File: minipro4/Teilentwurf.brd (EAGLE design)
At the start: 105.1 x 94.6 mm, 90 parts, among them IC1 MEGA8-P, IC2 FT232RL_ADAPTER, IC3 78L08Z, IC4 4051N, IC5 TL082P, IC6 4051N, IC7 TL082P, J1 HOHLSTECKER, Q2 BS170, Q3 BS170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

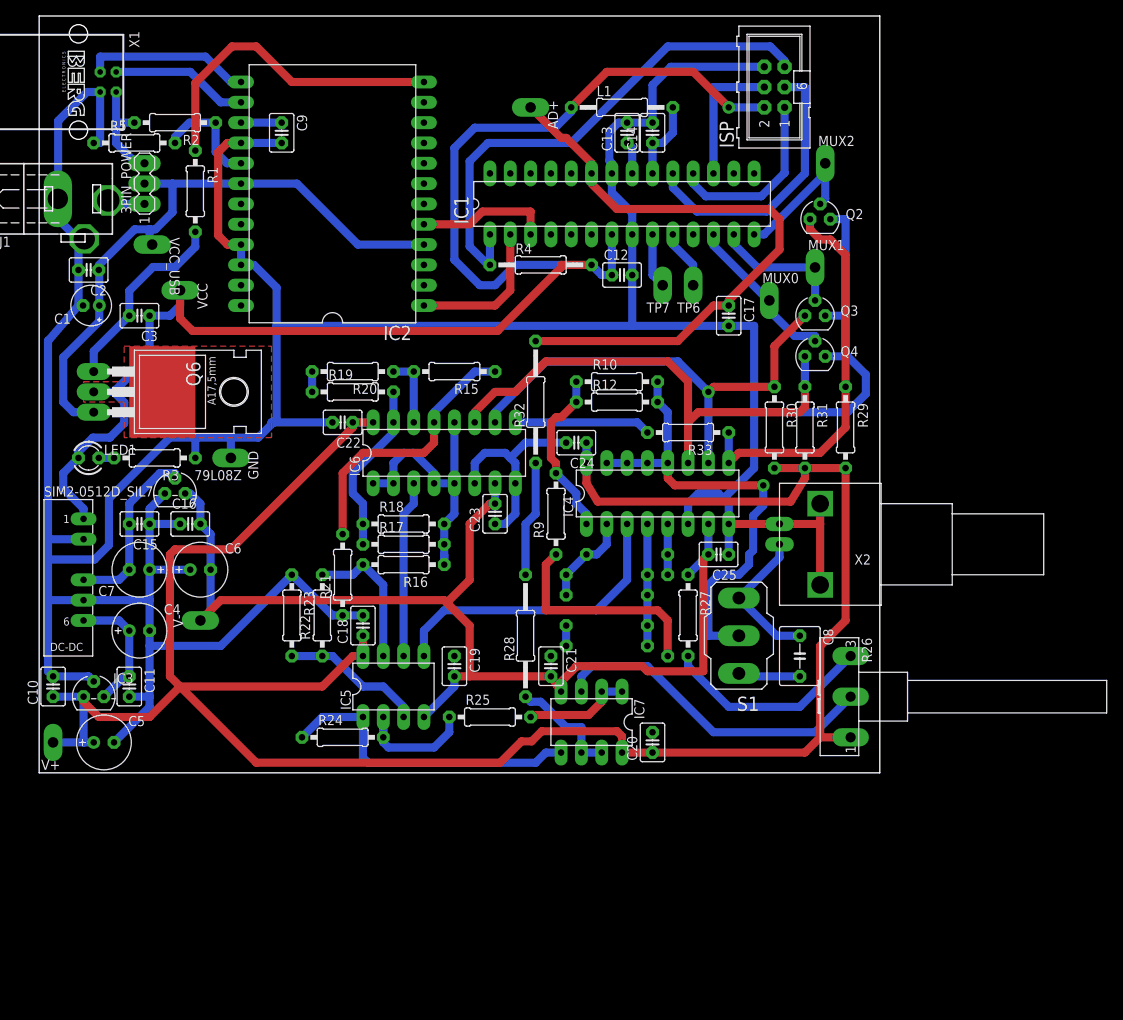
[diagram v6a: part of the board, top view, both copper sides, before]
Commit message: Added ground plane
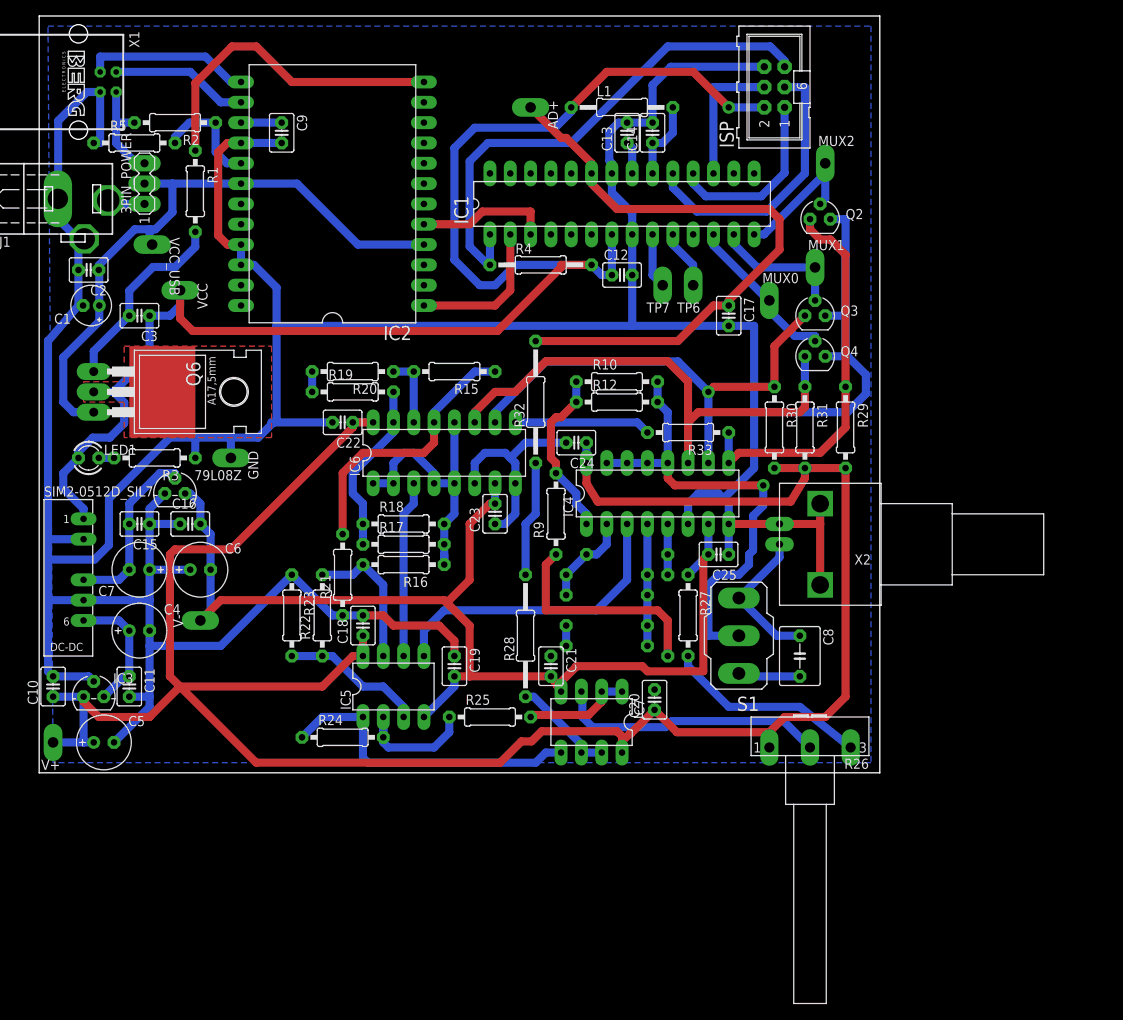
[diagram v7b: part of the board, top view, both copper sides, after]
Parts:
- moved R26 6.35 mm to (96.5, 2.54), turned to 90 degrees
- moved C20 5.34 mm to (77.1, 7.24)
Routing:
- net GND: track 531.0 -> 545.6 mm
- net N$39: track 41.3 -> 33.9 mm
- net V+: track 283.0 -> 281.7 mm
- net N$40: track 14.3 -> 13.0 mm
- net N$38: track 26.3 -> 25.5 mm
- added copper zone on layer 16, net GND
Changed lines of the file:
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@@
 <setting verticaltext="up"/>
 </settings>
-<grid distance="25" unitdist="mil" unit="mil" style="lines" multiple="1" display="no" altdistance="0.3175" altunitdist="mm" altunit="mm"/>
+<grid distance="10" unitdist="mil" unit="mil" style="lines" multiple="1" display="no" altdistance="0.3175" altunitdist="mm" altunit="mm"/>
 <layers>
 <layer number="1" name="Top" color="4" fill="1" visible="yes" active="yes"/>
@@
 <element name="IC7" library="03_device-library" package="DIL08" value="TL082P" x="69.215" y="4.445" rot="R180"/>
 <element name="R25" library="03_device-library" package="0207/10" value="100k" x="56.515" y="5.08"/>
-<element name="R26" library="03_device-library" package="POT" value="100k" x="100.33" y="7.62" rot="R180"/>
+<element name="R26" library="03_device-library" package="POT" value="100k" x="96.52" y="2.54" rot="R90"/>
 <element name="R27" library="03_device-library" package="0207/10" value="22k" x="81.28" y="17.78" rot="R270"/>
 <element name="R28" library="03_device-library" package="0207/15" value="8k2" x="60.96" y="15.24" rot="R90"/>
@@
 <element name="C18" library="03_device-library" package="C025-030X050" value="100nF" x="40.64" y="16.51" rot="R90"/>
 <element name="C19" library="03_device-library" package="C025-030X050" value="100nF" x="52.07" y="11.43" rot="R270"/>
-<element name="C20" library="03_device-library" package="C025-030X050" value="100nF" x="76.835" y="1.905" rot="R90"/>
+<element name="C20" library="03_device-library" package="C025-030X050" value="100nF" x="77.089" y="7.239" rot="R90"/>
 <element name="C21" library="03_device-library" package="C025-030X050" value="100nF" x="64.135" y="11.43" rot="R270"/>
 <element name="C22" library="03_device-library" package="C025-030X050" value="100nF" x="38.1" y="41.91" rot="R180"/>
@@
 <wire x1="59.69" y1="30.48" x2="58.42" y2="29.21" width="1.016" layer="16"/>
 <wire x1="58.42" y1="29.21" x2="57.15" y2="29.21" width="1.016" layer="16"/>
-<wire x1="66.04" y1="16.51" x2="58.42" y2="29.21" width="0" layer="19" extent="16-16"/>
-<wire x1="64.135" y1="12.7" x2="66.04" y2="13.97" width="0" layer="19" extent="1-1"/>
-<wire x1="52.07" y1="12.7" x2="64.135" y2="12.7" width="0" layer="19" extent="1-1"/>
-<wire x1="40.64" y1="17.78" x2="52.07" y2="12.7" width="0" layer="19" extent="1-1"/>
-<wire x1="76.835" y1="3.175" x2="66.04" y2="13.97" width="0" layer="19" extent="1-1"/>
+<polygon width="0.8128" layer="16" isolate="0.254" rank="2">
+<vertex x="1.27" y="91.44"/>
+<vertex x="104.14" y="91.44"/>
+<vertex x="104.14" y="-0.635"/>
+<vertex x="1.905" y="-0.635"/>
+</polygon>
+<wire x1="52.07" y1="12.7" x2="52.07" y2="14.605" width="1.016" layer="1"/>
+<wire x1="52.07" y1="14.605" x2="50.165" y2="16.51" width="1.016" layer="1"/>
+<wire x1="50.165" y1="16.51" x2="44.45" y2="16.51" width="1.016" layer="1"/>
+<wire x1="44.45" y1="16.51" x2="43.18" y2="17.78" width="1.016" layer="1"/>
+<wire x1="43.18" y1="17.78" x2="40.64" y2="17.78" width="1.016" layer="1"/>
 </signal>
 <signal name="N$20">
@@
 <wire x1="69.977" y1="32.004" x2="68.58" y2="34.29" width="1.016" layer="1"/>
 <wire x1="68.58" y1="34.29" x2="68.58" y2="36.83" width="1.016" layer="1"/>
-<wire x1="100.965" y1="36.195" x2="100.965" y2="17.145" width="1.016" layer="1"/>
-<wire x1="97.79" y1="13.97" x2="97.79" y2="2.54" width="1.016" layer="1"/>
-<wire x1="97.79" y1="2.54" x2="101.6" y2="2.54" width="1.016" layer="1"/>
-<wire x1="100.965" y1="17.145" x2="97.79" y2="13.97" width="1.016" layer="1"/>
+<wire x1="100.965" y1="36.195" x2="100.965" y2="7.62" width="1.016" layer="1"/>
 <wire x1="95.885" y1="36.195" x2="95.885" y2="34.925" width="1.016" layer="1"/>
 <wire x1="95.885" y1="34.925" x2="94.107" y2="32.004" width="1.016" layer="1"/>
@@
 <wire x1="16.51" y1="25.4" x2="16.51" y2="10.16" width="1.016" layer="1"/>
 <wire x1="16.51" y1="10.16" x2="17.78" y2="8.89" width="1.016" layer="1"/>
-<wire x1="76.835" y1="0.635" x2="95.885" y2="0.635" width="1.016" layer="1"/>
-<wire x1="95.885" y1="0.635" x2="97.79" y2="2.54" width="1.016" layer="1"/>
 <wire x1="39.37" y1="41.91" x2="39.37" y2="41.275" width="1.016" layer="1"/>
 <wire x1="39.37" y1="41.275" x2="24.13" y2="26.035" width="1.016" layer="1"/>
-<wire x1="73.025" y1="0.635" x2="73.025" y2="2.667" width="1.016" layer="1"/>
+<wire x1="73.025" y1="0.635" x2="73.025" y2="2.032" width="1.016" layer="1"/>
+<wire x1="73.025" y1="2.032" x2="73.025" y2="2.667" width="1.016" layer="1"/>
 <wire x1="60.452" y1="2.032" x2="57.785" y2="-0.635" width="1.016" layer="1"/>
 <wire x1="57.785" y1="-0.635" x2="27.305" y2="-0.635" width="1.016" layer="1"/>
 <wire x1="27.305" y1="-0.635" x2="17.78" y2="8.89" width="1.016" layer="1"/>
-<wire x1="73.025" y1="0.635" x2="76.835" y2="0.635" width="1.016" layer="1"/>
 <wire x1="73.025" y1="2.667" x2="72.39" y2="3.302" width="1.016" layer="1"/>
 <wire x1="72.39" y1="3.302" x2="62.992" y2="3.302" width="1.016" layer="1"/>
 <wire x1="62.992" y1="3.302" x2="61.722" y2="2.032" width="1.016" layer="1"/>
 <wire x1="61.722" y1="2.032" x2="60.452" y2="2.032" width="1.016" layer="1"/>
+<wire x1="91.44" y1="1.27" x2="91.44" y2="3.175" width="1.016" layer="1"/>
+<wire x1="91.44" y1="3.175" x2="93.345" y2="5.08" width="1.016" layer="1"/>
+<wire x1="100.965" y1="7.62" x2="98.425" y2="5.08" width="1.016" layer="1"/>
+<wire x1="98.425" y1="5.08" x2="93.345" y2="5.08" width="1.016" layer="1"/>
+<wire x1="77.089" y1="5.969" x2="74.168" y2="3.048" width="1.016" layer="1"/>
+<wire x1="74.168" y1="3.048" x2="74.041" y2="3.048" width="1.016" layer="1"/>
+<wire x1="74.041" y1="3.048" x2="73.025" y2="2.032" width="1.016" layer="1"/>
+<wire x1="91.44" y1="3.175" x2="79.883" y2="3.175" width="1.016" layer="1"/>
+<wire x1="79.883" y1="3.175" x2="77.089" y2="5.969" width="1.016" layer="1"/>
 </signal>
 <signal name="V-">
@@
 <wire x1="53.975" y1="29.21" x2="53.975" y2="22.225" width="1.016" layer="1"/>
 <wire x1="53.975" y1="22.225" x2="51.1175" y2="19.3675" width="1.016" layer="1"/>
-<wire x1="52.07" y1="10.16" x2="64.135" y2="10.16" width="1.016" layer="1"/>
+<wire x1="52.07" y1="10.16" x2="53.975" y2="10.16" width="1.016" layer="1"/>
+<wire x1="53.975" y1="10.16" x2="64.135" y2="10.16" width="1.016" layer="1"/>
 <wire x1="64.135" y1="10.16" x2="64.9165375" y2="8.98769375" width="1.016" layer="1"/>
 <wire x1="64.9165375" y1="8.98769375" x2="65.405" y2="8.255" width="1.016" layer="1"/>
@@
 <wire x1="67.31" y1="11.43" x2="67.31" y2="11.38115625" width="1.016" layer="1"/>
 <wire x1="67.31" y1="11.38115625" x2="64.9165375" y2="8.98769375" width="1.016" layer="1"/>
-<wire x1="53.975" y1="10.16" x2="52.07" y2="10.16" width="0" layer="19" extent="1-1"/>
 </signal>
 <signal name="N$4">
@@
 <wire x1="81.28" y1="12.7" x2="81.28" y2="11.43" width="1.016" layer="16"/>
 <wire x1="81.28" y1="11.43" x2="86.36" y2="6.35" width="1.016" layer="16"/>
-<wire x1="95.25" y1="6.35" x2="101.6" y2="12.7" width="1.016" layer="16"/>
+<wire x1="95.25" y1="6.35" x2="101.6" y2="1.27" width="1.016" layer="16"/>
 <wire x1="86.36" y1="6.35" x2="95.25" y2="6.35" width="1.016" layer="16"/>
 </signal>
@@
 <contactref element="R26" pad="2"/>
 <contactref element="IC7" pad="3"/>
-<wire x1="76.2" y1="11.43" x2="84.455" y2="3.175" width="1.016" layer="16"/>
-<wire x1="84.455" y1="3.175" x2="97.155" y2="3.175" width="1.016" layer="16"/>
-<wire x1="97.155" y1="3.175" x2="101.6" y2="7.62" width="1.016" layer="16"/>
-<wire x1="67.945" y1="8.255" x2="67.945" y2="10.16" width="1.016" layer="16"/>
-<wire x1="76.2" y1="11.43" x2="69.215" y2="11.43" width="1.016" layer="16"/>
-<wire x1="69.215" y1="11.43" x2="67.945" y2="10.16" width="1.016" layer="16"/>
+<wire x1="96.52" y1="1.27" x2="93.218" y2="4.572" width="1.016" layer="16"/>
+<wire x1="93.218" y1="4.572" x2="79.248" y2="4.572" width="1.016" layer="16"/>
+<wire x1="79.248" y1="4.572" x2="78.486" y2="3.81" width="1.016" layer="16"/>
+<wire x1="78.486" y1="3.81" x2="69.342" y2="3.81" width="1.016" layer="16"/>
+<wire x1="69.342" y1="3.81" x2="68.072" y2="5.08" width="1.016" layer="16"/>
+<wire x1="68.072" y1="5.08" x2="68.072" y2="8.128" width="1.016" layer="16"/>
+<wire x1="68.072" y1="8.128" x2="67.945" y2="8.255" width="1.016" layer="16"/>
 </signal>
 <signal name="N$40">
@@
 <contactref element="R28" pad="1"/>
 <wire x1="70.485" y1="0.635" x2="67.945" y2="0.635" width="1.016" layer="16"/>
-<wire x1="67.945" y1="0.635" x2="67.945" y2="3.81" width="1.016" layer="16"/>
-<wire x1="67.945" y1="3.81" x2="66.04" y2="3.81" width="1.016" layer="16"/>
-<wire x1="66.04" y1="3.81" x2="62.865" y2="6.985" width="1.016" layer="16"/>
-<wire x1="62.865" y1="6.985" x2="61.595" y2="6.985" width="1.016" layer="16"/>
-<wire x1="61.595" y1="6.985" x2="60.96" y2="7.62" width="1.016" layer="16"/>
+<wire x1="67.945" y1="0.635" x2="67.945" y2="1.651" width="1.016" layer="16"/>
+<wire x1="67.945" y1="1.651" x2="61.976" y2="7.62" width="1.016" layer="16"/>
+<wire x1="61.976" y1="7.62" x2="60.96" y2="7.62" width="1.016" layer="16"/>
 </signal>
 <signal name="N$41">

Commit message: Layout
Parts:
- moved C20 6.67 mm to (79.1, 0.89), turned to 180 degrees
- moved R25 6.35 mm to (51.4, 1.27)
- moved R28 2.54 mm to (58.4, 15.2)
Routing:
- net GND: track 545.6 -> 0.00 mm
- net N$36: track 16.9 -> 2.54 mm
- net N$31: track 34.2 -> 26.5 mm
- net N$37: track 13.5 -> 19.8 mm
- net N$40: track 13.0 -> 15.7 mm
- net V+: track 281.7 -> 279.8 mm
- net N$27: track 17.9 -> 19.5 mm
